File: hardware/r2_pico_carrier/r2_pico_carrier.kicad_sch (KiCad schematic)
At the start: 67 parts, among them J1 5V in, J2 OLED HS96L03W2C03, SW1 display, U1 PCA9517A

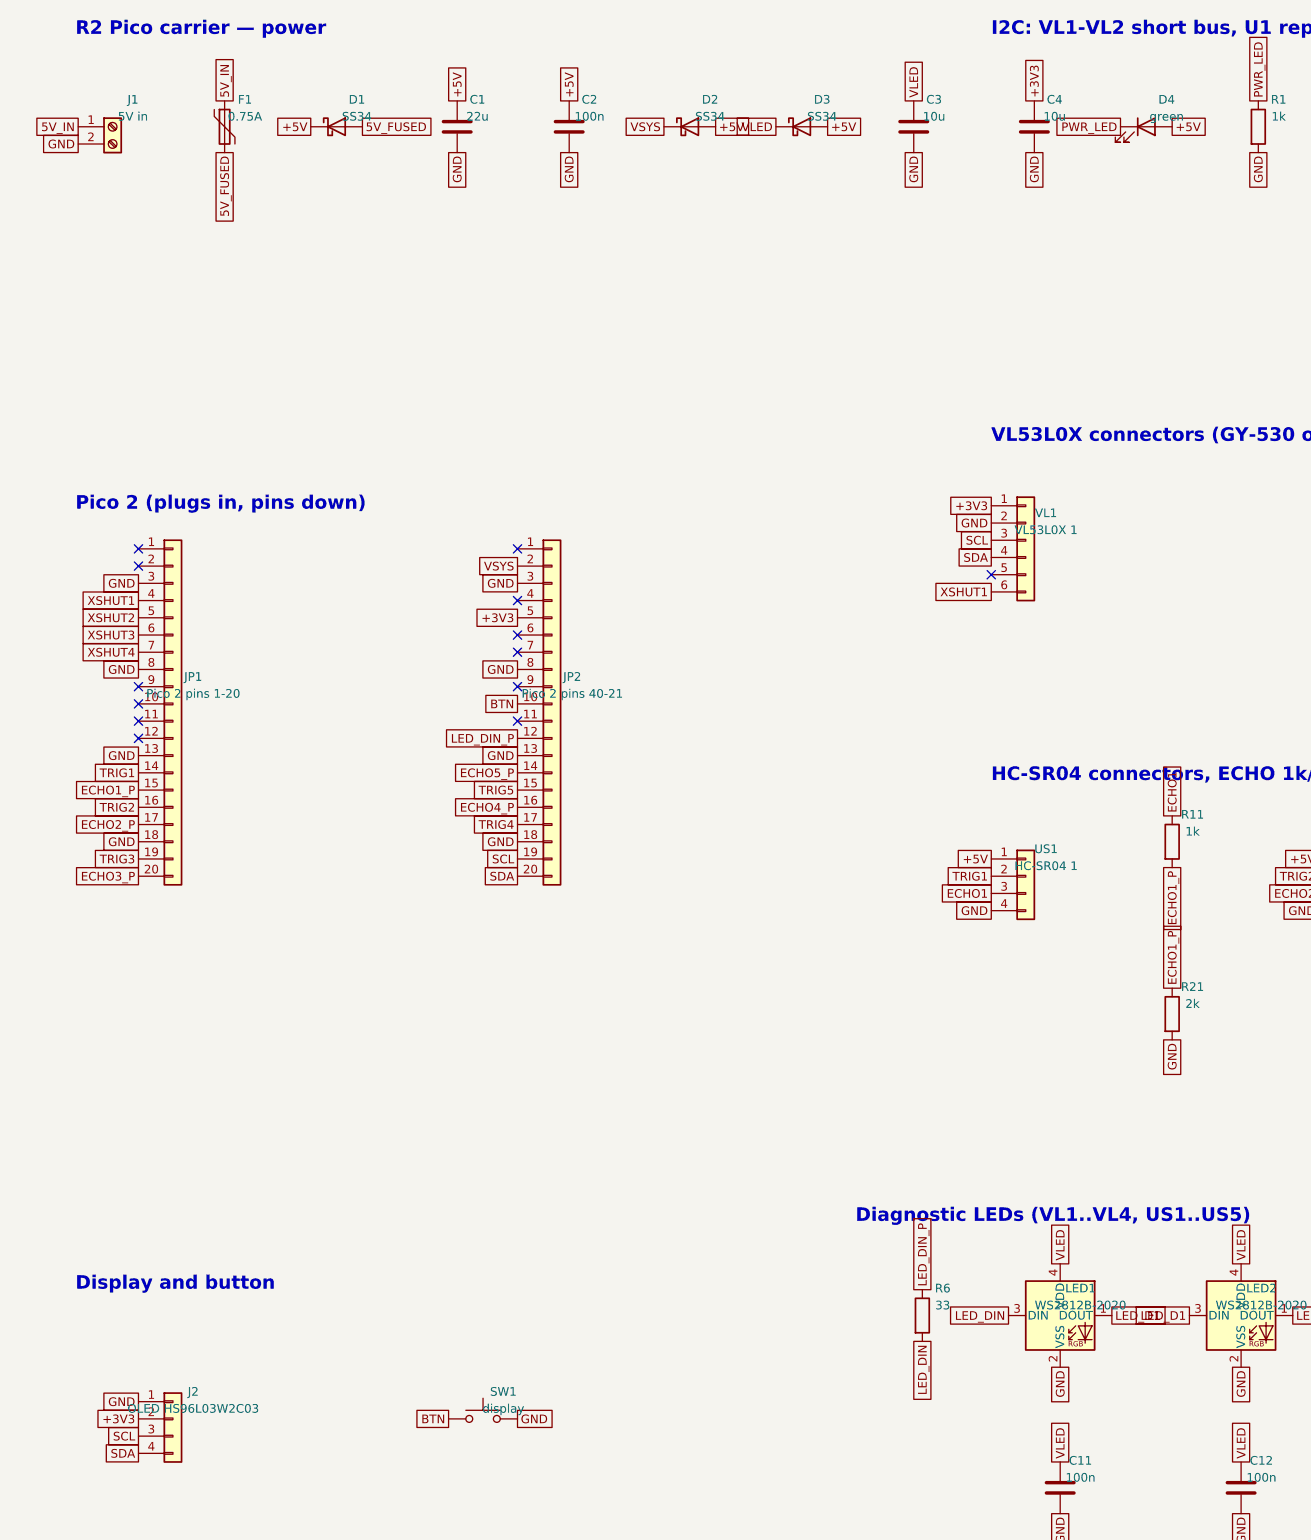
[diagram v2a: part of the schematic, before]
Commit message: Carrier board: in-stock Pico sockets (C2905423) and power LED (C2286, red); OLED plugs into a 4-pin socket (C2718488)
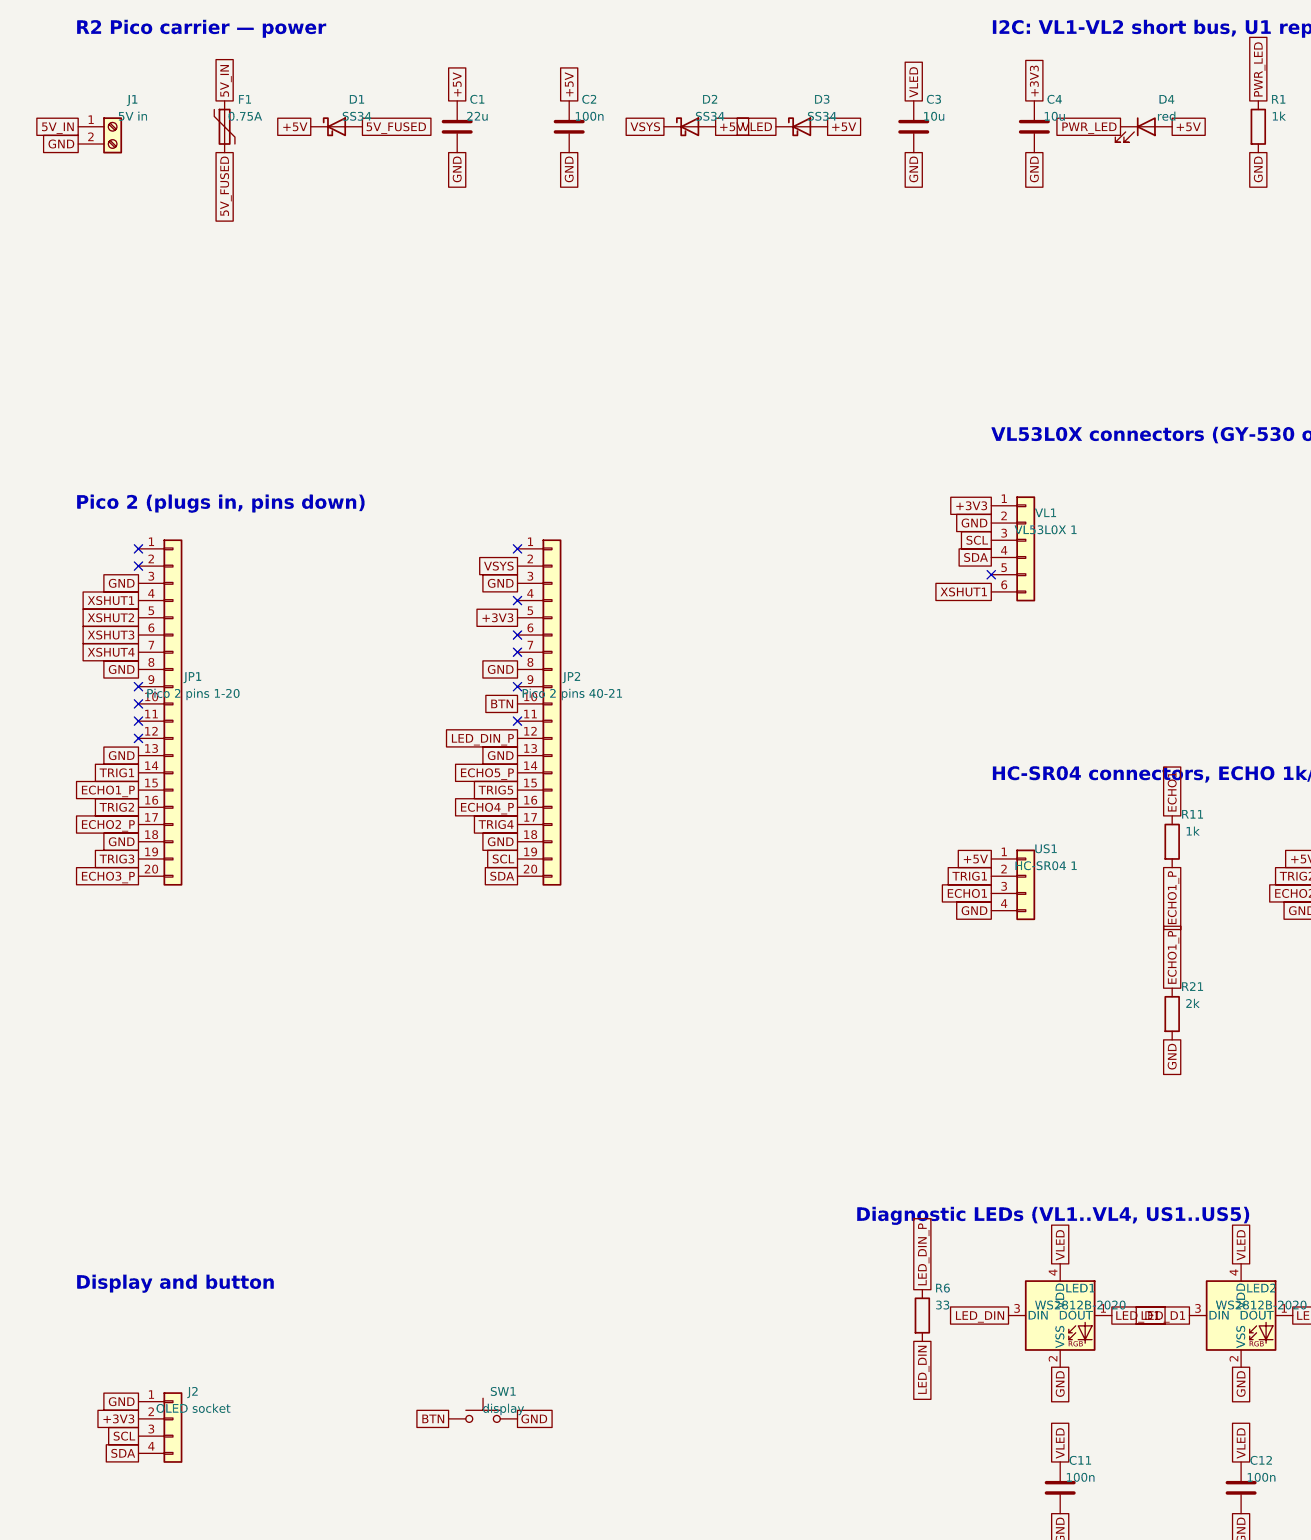
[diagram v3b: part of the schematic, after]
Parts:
- D4: value green -> red; LCSC C72043 -> C2286
- J2: value OLED HS96L03W2C03 -> OLED socket; footprint Connector_PinHeader_2.54mm:PinHeader_1x04_P2.54mm_Vertical -> Connector_PinSocket_2.54mm:PinSocket_1x04_P2.54mm_Vertical; LCSC C5248080 -> C2718488
- JP1, JP2: LCSC C50984 -> C2905423
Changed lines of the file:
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@@
 (kicad_sch (version 20250114) (generator "r2_pico_carrier_gen") (generator_version "10.0") (paper "A3") (title_block (title "R2 Pico carrier") (date "2026-10-27") (rev "A") (company "ROS2D2 · Astromech Spain") (comment 1 "Generated by gen/make_sch.py from gen/parts.py"))
-(symbol (lib_id "Connector_Generic:Conn_01x20") (at 39.37 124.46 0) (unit 1) (exclude_from_sim no) (in_bom yes) (on_board yes) (dnp no) (property "Reference" "JP1" (at 42.37 120.46000000000001 0) (effects (font (size 1.27 1.27)))) (property "Value" "Pico 2 pins 1-20" (at 42.37 122.96000000000001 0) (effects (font (size 1.27 1.27)))) (property "Footprint" "Connector_PinSocket_2.54mm:PinSocket_1x20_P2.54mm_Vertical" (at 42.37 125.46000000000001 0) (effects (font (size 1.27 1.27)) (hide yes))) (property "Datasheet" "" (at 42.37 127.96000000000001 0) (effects (font (size 1.27 1.27)) (hide yes))) (property "LCSC" "C50984" (at 42.37 130.46 0) (effects (font (size 1.27 1.27)) (hide yes))) (pin "1") (pin "2") (pin "3") (pin "4") (pin "5") (pin "6") (pin "7") (pin "8") (pin "9") (pin "10") (pin "11") (pin "12") (pin "13") (pin "14") (pin "15") (pin "16") (pin "17") (pin "18") (pin "19") (pin "20") (instances (project "r2_pico_carrier" (path "/1e5ddbbd-1ed4-52be-93d8-b73224ab9bea" (reference "JP1") (unit 1)))))
+(symbol (lib_id "Connector_Generic:Conn_01x20") (at 39.37 124.46 0) (unit 1) (exclude_from_sim no) (in_bom yes) (on_board yes) (dnp no) (property "Reference" "JP1" (at 42.37 120.46000000000001 0) (effects (font (size 1.27 1.27)))) (property "Value" "Pico 2 pins 1-20" (at 42.37 122.96000000000001 0) (effects (font (size 1.27 1.27)))) (property "Footprint" "Connector_PinSocket_2.54mm:PinSocket_1x20_P2.54mm_Vertical" (at 42.37 125.46000000000001 0) (effects (font (size 1.27 1.27)) (hide yes))) (property "Datasheet" "" (at 42.37 127.96000000000001 0) (effects (font (size 1.27 1.27)) (hide yes))) (property "LCSC" "C2905423" (at 42.37 130.46 0) (effects (font (size 1.27 1.27)) (hide yes))) (pin "1") (pin "2") (pin "3") (pin "4") (pin "5") (pin "6") (pin "7") (pin "8") (pin "9") (pin "10") (pin "11") (pin "12") (pin "13") (pin "14") (pin "15") (pin "16") (pin "17") (pin "18") (pin "19") (pin "20") (instances (project "r2_pico_carrier" (path "/1e5ddbbd-1ed4-52be-93d8-b73224ab9bea" (reference "JP1") (unit 1)))))
 (no_connect (at 34.29 101.60))
 (no_connect (at 34.29 104.14))
@@
 (global_label "TRIG3" (shape passive) (at 34.29 147.32 180) (fields_autoplaced yes) (effects (font (size 1.27 1.27)) (justify right)))
 (global_label "ECHO3_P" (shape passive) (at 34.29 149.86 180) (fields_autoplaced yes) (effects (font (size 1.27 1.27)) (justify right)))
-(symbol (lib_id "Connector_Generic:Conn_01x20") (at 95.25 124.46 0) (unit 1) (exclude_from_sim no) (in_bom yes) (on_board yes) (dnp no) (property "Reference" "JP2" (at 98.25 120.46000000000001 0) (effects (font (size 1.27 1.27)))) (property "Value" "Pico 2 pins 40-21" (at 98.25 122.96000000000001 0) (effects (font (size 1.27 1.27)))) (property "Footprint" "Connector_PinSocket_2.54mm:PinSocket_1x20_P2.54mm_Vertical" (at 98.25 125.46000000000001 0) (effects (font (size 1.27 1.27)) (hide yes))) (property "Datasheet" "" (at 98.25 127.96000000000001 0) (effects (font (size 1.27 1.27)) (hide yes))) (property "LCSC" "C50984" (at 98.25 130.46 0) (effects (font (size 1.27 1.27)) (hide yes))) (pin "1") (pin "2") (pin "3") (pin "4") (pin "5") (pin "6") (pin "7") (pin "8") (pin "9") (pin "10") (pin "11") (pin "12") (pin "13") (pin "14") (pin "15") (pin "16") (pin "17") (pin "18") (pin "19") (pin "20") (instances (project "r2_pico_carrier" (path "/1e5ddbbd-1ed4-52be-93d8-b73224ab9bea" (reference "JP2") (unit 1)))))
+(symbol (lib_id "Connector_Generic:Conn_01x20") (at 95.25 124.46 0) (unit 1) (exclude_from_sim no) (in_bom yes) (on_board yes) (dnp no) (property "Reference" "JP2" (at 98.25 120.46000000000001 0) (effects (font (size 1.27 1.27)))) (property "Value" "Pico 2 pins 40-21" (at 98.25 122.96000000000001 0) (effects (font (size 1.27 1.27)))) (property "Footprint" "Connector_PinSocket_2.54mm:PinSocket_1x20_P2.54mm_Vertical" (at 98.25 125.46000000000001 0) (effects (font (size 1.27 1.27)) (hide yes))) (property "Datasheet" "" (at 98.25 127.96000000000001 0) (effects (font (size 1.27 1.27)) (hide yes))) (property "LCSC" "C2905423" (at 98.25 130.46 0) (effects (font (size 1.27 1.27)) (hide yes))) (pin "1") (pin "2") (pin "3") (pin "4") (pin "5") (pin "6") (pin "7") (pin "8") (pin "9") (pin "10") (pin "11") (pin "12") (pin "13") (pin "14") (pin "15") (pin "16") (pin "17") (pin "18") (pin "19") (pin "20") (instances (project "r2_pico_carrier" (path "/1e5ddbbd-1ed4-52be-93d8-b73224ab9bea" (reference "JP2") (unit 1)))))
 (no_connect (at 90.17 101.60))
 (global_label "VSYS" (shape passive) (at 90.17 104.14 180) (fields_autoplaced yes) (effects (font (size 1.27 1.27)) (justify right)))
@@
 (global_label "+3V3" (shape passive) (at 166.37 35.56 90) (fields_autoplaced yes) (effects (font (size 1.27 1.27)) (justify left)))
 (global_label "GND" (shape passive) (at 166.37 43.18 270) (fields_autoplaced yes) (effects (font (size 1.27 1.27)) (justify right)))
-(symbol (lib_id "Device:LED") (at 182.88 39.37 0) (unit 1) (exclude_from_sim no) (in_bom yes) (on_board yes) (dnp no) (property "Reference" "D4" (at 185.88 35.37 0) (effects (font (size 1.27 1.27)))) (property "Value" "green" (at 185.88 37.87 0) (effects (font (size 1.27 1.27)))) (property "Footprint" "LED_SMD:LED_0603_1608Metric" (at 185.88 40.37 0) (effects (font (size 1.27 1.27)) (hide yes))) (property "Datasheet" "" (at 185.88 42.87 0) (effects (font (size 1.27 1.27)) (hide yes))) (property "LCSC" "C72043" (at 185.88 45.37 0) (effects (font (size 1.27 1.27)) (hide yes))) (pin "1") (pin "2") (instances (project "r2_pico_carrier" (path "/1e5ddbbd-1ed4-52be-93d8-b73224ab9bea" (reference "D4") (unit 1)))))
+(symbol (lib_id "Device:LED") (at 182.88 39.37 0) (unit 1) (exclude_from_sim no) (in_bom yes) (on_board yes) (dnp no) (property "Reference" "D4" (at 185.88 35.37 0) (effects (font (size 1.27 1.27)))) (property "Value" "red" (at 185.88 37.87 0) (effects (font (size 1.27 1.27)))) (property "Footprint" "LED_SMD:LED_0603_1608Metric" (at 185.88 40.37 0) (effects (font (size 1.27 1.27)) (hide yes))) (property "Datasheet" "" (at 185.88 42.87 0) (effects (font (size 1.27 1.27)) (hide yes))) (property "LCSC" "C2286" (at 185.88 45.37 0) (effects (font (size 1.27 1.27)) (hide yes))) (pin "1") (pin "2") (instances (project "r2_pico_carrier" (path "/1e5ddbbd-1ed4-52be-93d8-b73224ab9bea" (reference "D4") (unit 1)))))
 (global_label "PWR_LED" (shape passive) (at 179.07 39.37 180) (fields_autoplaced yes) (effects (font (size 1.27 1.27)) (justify right)))
 (global_label "+5V" (shape passive) (at 186.69 39.37 0) (fields_autoplaced yes) (effects (font (size 1.27 1.27)) (justify left)))
@@
 (global_label "VLED" (shape passive) (at 386.08 236.22 90) (fields_autoplaced yes) (effects (font (size 1.27 1.27)) (justify left)))
 (global_label "GND" (shape passive) (at 386.08 243.84 270) (fields_autoplaced yes) (effects (font (size 1.27 1.27)) (justify right)))
-(symbol (lib_id "Connector_Generic:Conn_01x04") (at 39.37 229.87 0) (unit 1) (exclude_from_sim no) (in_bom yes) (on_board yes) (dnp no) (property "Reference" "J2" (at 42.37 225.87 0) (effects (font (size 1.27 1.27)))) (property "Value" "OLED HS96L03W2C03" (at 42.37 228.37 0) (effects (font (size 1.27 1.27)))) (property "Footprint" "Connector_PinHeader_2.54mm:PinHeader_1x04_P2.54mm_Vertical" (at 42.37 230.87 0) (effects (font (size 1.27 1.27)) (hide yes))) (property "Datasheet" "" (at 42.37 233.37 0) (effects (font (size 1.27 1.27)) (hide yes))) (property "LCSC" "C5248080" (at 42.37 235.87 0) (effects (font (size 1.27 1.27)) (hide yes))) (pin "1") (pin "2") (pin "3") (pin "4") (instances (project "r2_pico_carrier" (path "/1e5ddbbd-1ed4-52be-93d8-b73224ab9bea" (reference "J2") (unit 1)))))
+(symbol (lib_id "Connector_Generic:Conn_01x04") (at 39.37 229.87 0) (unit 1) (exclude_from_sim no) (in_bom yes) (on_board yes) (dnp no) (property "Reference" "J2" (at 42.37 225.87 0) (effects (font (size 1.27 1.27)))) (property "Value" "OLED socket" (at 42.37 228.37 0) (effects (font (size 1.27 1.27)))) (property "Footprint" "Connector_PinSocket_2.54mm:PinSocket_1x04_P2.54mm_Vertical" (at 42.37 230.87 0) (effects (font (size 1.27 1.27)) (hide yes))) (property "Datasheet" "" (at 42.37 233.37 0) (effects (font (size 1.27 1.27)) (hide yes))) (property "LCSC" "C2718488" (at 42.37 235.87 0) (effects (font (size 1.27 1.27)) (hide yes))) (pin "1") (pin "2") (pin "3") (pin "4") (instances (project "r2_pico_carrier" (path "/1e5ddbbd-1ed4-52be-93d8-b73224ab9bea" (reference "J2") (unit 1)))))
 (global_label "GND" (shape passive) (at 34.29 227.33 180) (fields_autoplaced yes) (effects (font (size 1.27 1.27)) (justify right)))
 (global_label "+3V3" (shape passive) (at 34.29 229.87 180) (fields_autoplaced yes) (effects (font (size 1.27 1.27)) (justify right)))

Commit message: Carrier board: WS2812B-2020-V6 (in stock) for the diagnostic LEDs
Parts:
- LED1, LED2, LED3, LED4, LED5, LED6, LED7, LED8, LED9: LCSC C965555 -> C52917434

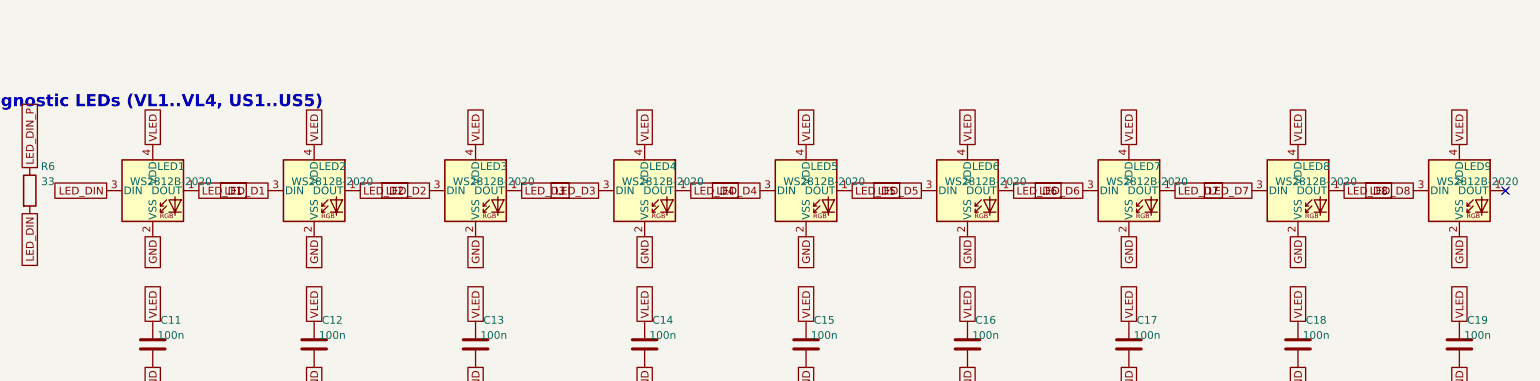
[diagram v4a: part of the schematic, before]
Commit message: Carrier board: classic 5050 WS2812B (C2874885) for the diagnostic LEDs
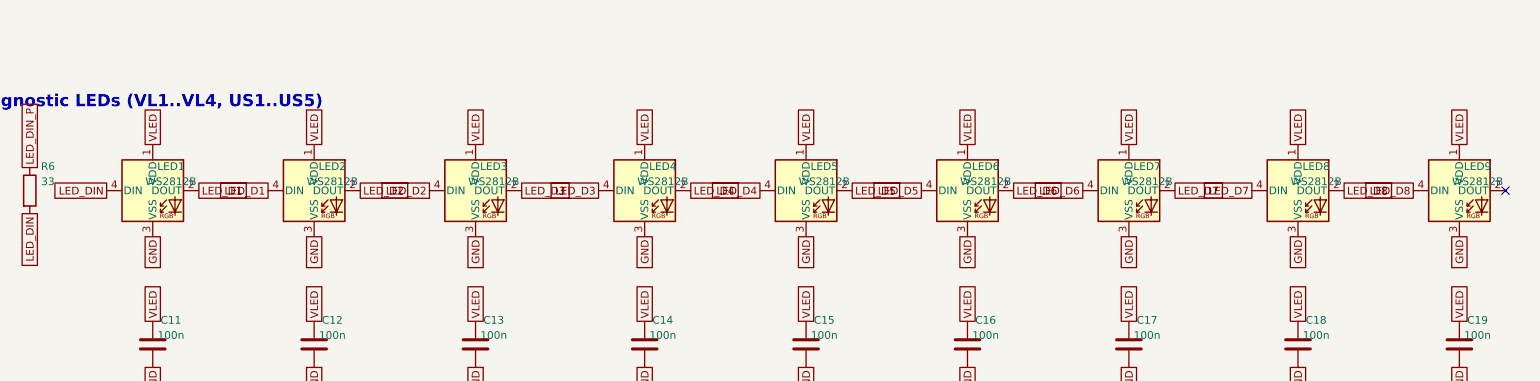
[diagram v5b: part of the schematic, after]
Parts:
- LED1, LED2, LED3, LED4, LED5, LED6, LED7, LED8, LED9: value WS2812B-2020 -> WS2812B; footprint LED_SMD:LED_WS2812B-2020_PLCC4_2.0x2.0mm -> LED_SMD:LED_WS2812B_PLCC4_5.0x5.0mm_P3.2mm; symbol LED:WS2812B-2020 -> LED:WS2812B; LCSC C52917434 -> C2874885
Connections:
- net GND: now also LED1.3 (VSS), LED2.3 (VSS), LED3.3 (VSS), LED4.3 (VSS), LED5.3 (VSS), LED6.3 (VSS), LED7.3 (VSS), LED8.3 (VSS), LED9.3 (VSS); no longer LED1.2 (VSS), LED2.2 (VSS), LED3.2 (VSS), LED4.2 (VSS), LED5.2 (VSS), LED6.2 (VSS), LED7.2 (VSS), LED8.2 (VSS), LED9.2 (VSS)
- net LED_D1: now also LED1.2 (DOUT), LED2.4 (DIN); no longer LED1.1 (DOUT), LED2.3 (DIN)
- net LED_D2: now also LED2.2 (DOUT), LED3.4 (DIN); no longer LED2.1 (DOUT), LED3.3 (DIN)
- net LED_D3: now also LED3.2 (DOUT), LED4.4 (DIN); no longer LED3.1 (DOUT), LED4.3 (DIN)
- net LED_D4: now also LED4.2 (DOUT), LED5.4 (DIN); no longer LED4.1 (DOUT), LED5.3 (DIN)
- net LED_D5: now also LED5.2 (DOUT), LED6.4 (DIN); no longer LED5.1 (DOUT), LED6.3 (DIN)
- net LED_D6: now also LED6.2 (DOUT), LED7.4 (DIN); no longer LED6.1 (DOUT), LED7.3 (DIN)
- net LED_D7: now also LED7.2 (DOUT), LED8.4 (DIN); no longer LED7.1 (DOUT), LED8.3 (DIN)
- net LED_D8: now also LED8.2 (DOUT), LED9.4 (DIN); no longer LED8.1 (DOUT), LED9.3 (DIN)
- net LED_DIN: now also LED1.4 (DIN); no longer LED1.3 (DIN)
- net VLED: now also LED1.1 (VDD), LED2.1 (VDD), LED3.1 (VDD), LED4.1 (VDD), LED5.1 (VDD), LED6.1 (VDD), LED7.1 (VDD), LED8.1 (VDD), LED9.1 (VDD); no longer LED1.4 (VDD), LED2.4 (VDD), LED3.4 (VDD), LED4.4 (VDD), LED5.4 (VDD), LED6.4 (VDD), LED7.4 (VDD), LED8.4 (VDD), LED9.4 (VDD)
